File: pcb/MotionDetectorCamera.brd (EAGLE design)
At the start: 100 x 80 mm, 80 parts, among them U1 AT25XV041B-SSHV-T_AT25XV041B-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, U2 TPS62801X_TPS6280X, U3 TPS62801X_TPS6280X, U4 TPS6380X_TPS6380X, U5 LATTICE-SEMICONDUCTOR---ICE40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, U6 MICRON---MT48H32M16LFB4-6-IT: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, X1 CON-COAX_734120110, X10 CON-COAX_734120110, X2 CON-COAX_734120110, X3 CON-COAX_734120110, X4 CON-COAX_734120110, X5 CON-COAX_734120110, X6 CON-COAX_734120110, X7 CON-COAX_734120110, X8 CON-COAX_734120110, X9 CON-COAX_734120110, Y1 SIT8021AI-J4-XXS-12.000000E_S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

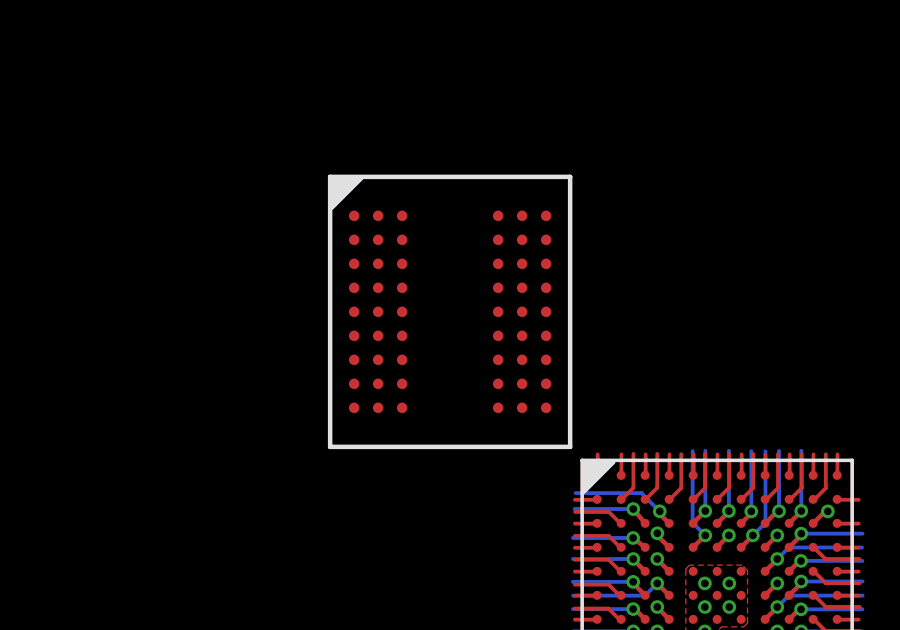
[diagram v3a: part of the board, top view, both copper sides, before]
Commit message: Broke out RAM pins
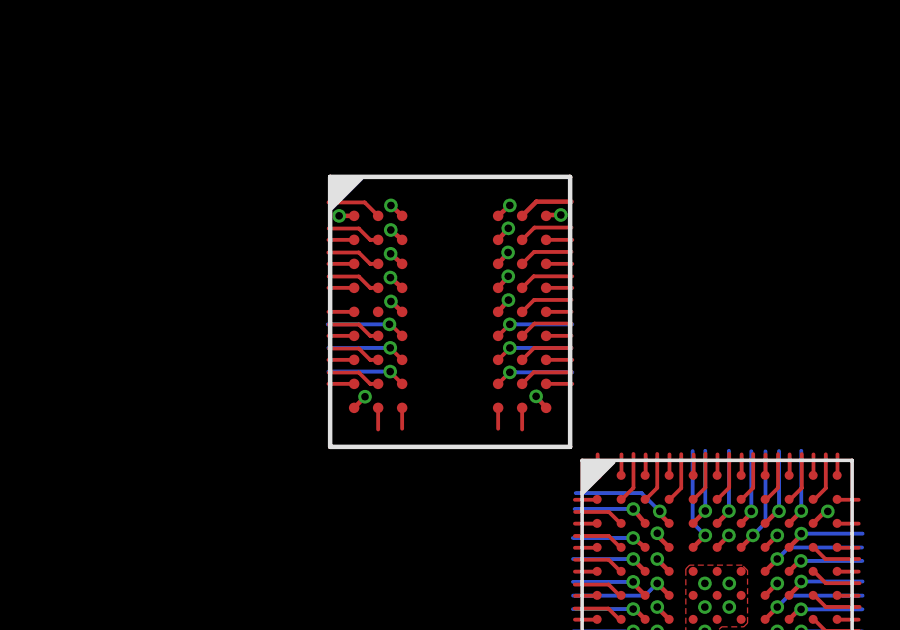
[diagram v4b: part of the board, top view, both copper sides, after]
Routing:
- net GND: track 7.50 -> 11.1 mm, vias 5 -> 12
- net 1V8: track 7.19 -> 10.8 mm, vias 5 -> 12
- net RAM_CKE: track 0.00 -> 2.64 mm, vias 0 -> 1
- net RAM_A6: track 0.00 -> 2.63 mm, vias 0 -> 1
- net RAM_CAS_: track 0.00 -> 2.63 mm, vias 0 -> 1
- net RAM_A0: track 0.00 -> 2.63 mm, vias 0 -> 1
- net RAM_A9: track 0.00 -> 2.62 mm, vias 0 -> 1
- net RAM_BA0: track 0.00 -> 2.62 mm, vias 0 -> 1
- net RAM_DQ0: track 0.00 -> 1.84 mm
- net RAM_DQ15: track 0.00 -> 1.84 mm
- net RAM_DQ6: track 0.00 -> 1.83 mm
- net RAM_DQ11: track 0.00 -> 1.82 mm
- net RAM_DQ2: track 0.00 -> 1.82 mm
- net RAM_RAS_: track 0.00 -> 1.82 mm
- net RAM_DQ4: track 0.00 -> 1.81 mm
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
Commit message: Commit before attempting to rotate RAM 45 degrees
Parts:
- moved U6 3.61 mm to (47.6, 48.5)

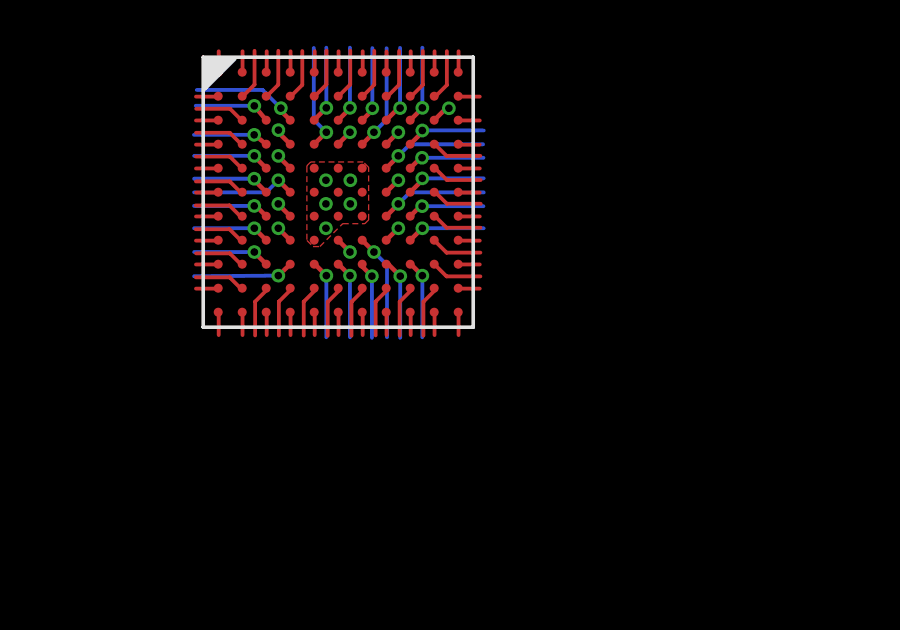
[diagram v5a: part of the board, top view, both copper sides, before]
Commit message: Connected VCC_SPI to 1V8
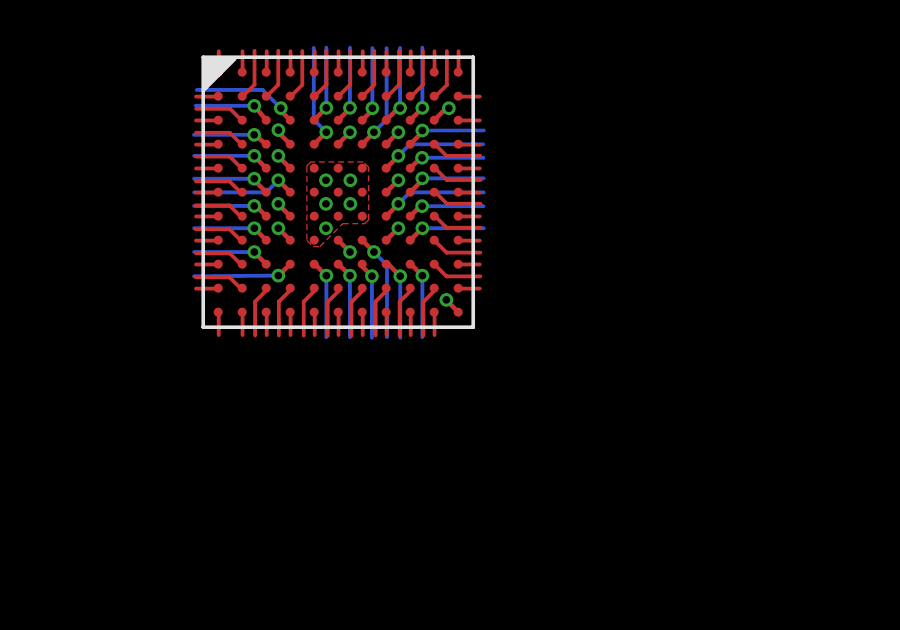
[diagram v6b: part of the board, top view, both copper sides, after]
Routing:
- net 1V8: vias 12 -> 13
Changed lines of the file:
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@@
 <wire x1="59.159" y1="34.984" x2="59.5503" y2="34.5927" width="0.1524" layer="1"/>
 <wire x1="59.5503" y1="34.5927" x2="59.5503" y2="34.58971875" width="0.1524" layer="1"/>
-<wire x1="63.17" y1="31.822" x2="63.17" y2="32.482" width="0.127" layer="1"/>
-<polygon width="0.1524" layer="15" rank="0">
-<vertex x="56.769" y="36.6014"/>
-<vertex x="56.769" y="35.9664"/>
-<vertex x="56.9722" y="35.7632"/>
-<vertex x="57.6326" y="35.7632"/>
-<vertex x="57.6326" y="31.75"/>
-<vertex x="59.9694" y="31.75"/>
-<vertex x="59.9694" y="35.0266"/>
-<vertex x="59.944" y="35.052"/>
-<vertex x="60.706" y="35.814"/>
-<vertex x="60.706" y="36.576"/>
-<vertex x="60.8076" y="36.6776"/>
-<vertex x="61.5188" y="36.6776"/>
-<vertex x="61.5188" y="37.2872"/>
-<vertex x="61.468" y="37.338"/>
-<vertex x="60.7568" y="37.338"/>
-<vertex x="59.2328" y="38.862"/>
-<vertex x="59.2328" y="39.3954"/>
-<vertex x="57.7088" y="39.3954"/>
-<vertex x="57.7088" y="38.5318"/>
-<vertex x="57.3786" y="38.2016"/>
-<vertex x="56.8198" y="38.2016"/>
-<vertex x="56.8198" y="37.5158"/>
-<vertex x="56.7944" y="37.4904"/>
-<vertex x="57.6072" y="37.4904"/>
-<vertex x="57.6326" y="37.465"/>
-<vertex x="57.6326" y="36.6522"/>
-<vertex x="57.5818" y="36.6014"/>
-</polygon>
 <wire x1="50.8428" y1="51.7232" x2="50.8721" y2="51.7525" width="0.1524" layer="1"/>
 <wire x1="50.8721" y1="51.7525" x2="51.4096" y2="51.7525" width="0.1524" layer="1"/>
@@
 <vertex x="51.8922" y="53.1876"/>
 </polygon>
-<wire x1="63.17" y1="32.482" x2="63.159" y2="32.584" width="0" layer="19" extent="1-1"/>
-<wire x1="59.5503" y1="34.58971875" x2="63.159" y2="32.584" width="0" layer="19" extent="1-1"/>
-<wire x1="50.8428" y1="45.3232" x2="57.1627" y2="37.7952" width="0" layer="19" extent="1-1"/>
-<wire x1="14.9834" y1="59.7408" x2="45.638790625" y2="51.328390625" width="0" layer="19" extent="16-16"/>
-<wire x1="14.9834" y1="60.7822" x2="14.9834" y2="59.7408" width="0" layer="19" extent="16-16"/>
+<wire x1="59.9694" y1="35.0266" x2="59.944" y2="35.052" width="0.1524" layer="15"/>
+<wire x1="63.159" y1="32.584" x2="62.7634" y2="32.9946" width="0.1524" layer="1"/>
+<via x="62.7634" y="32.9946" extent="1-16" drill="0.254"/>
+<polygon width="0.1524" layer="15" rank="0">
+<vertex x="56.769" y="36.6014"/>
+<vertex x="56.769" y="35.9664"/>
+<vertex x="56.9722" y="35.7632"/>
+<vertex x="57.6326" y="35.7632"/>
+<vertex x="57.6326" y="31.75"/>
+<vertex x="63.7032" y="31.75"/>
+<vertex x="63.8302" y="31.877"/>
+<vertex x="63.8302" y="33.5788"/>
+<vertex x="63.8048" y="33.6042"/>
+<vertex x="62.3305375" y="33.6042"/>
+<vertex x="60.706" y="35.2287375"/>
+<vertex x="60.706" y="36.576"/>
+<vertex x="60.8076" y="36.6776"/>
+<vertex x="61.5188" y="36.6776"/>
+<vertex x="61.5188" y="37.2872"/>
+<vertex x="61.468" y="37.338"/>
+<vertex x="60.7568" y="37.338"/>
+<vertex x="59.2328" y="38.862"/>
+<vertex x="59.2328" y="39.3954"/>
+<vertex x="57.7088" y="39.3954"/>
+<vertex x="57.7088" y="38.5318"/>
+<vertex x="57.3786" y="38.2016"/>
+<vertex x="56.8198" y="38.2016"/>
+<vertex x="56.8198" y="37.5158"/>
+<vertex x="56.7944" y="37.4904"/>
+<vertex x="57.6072" y="37.4904"/>
+<vertex x="57.6326" y="37.465"/>
+<vertex x="57.6326" y="36.6522"/>
+<vertex x="57.5818" y="36.6014"/>
+</polygon>
+<wire x1="14.9834" y1="59.7408" x2="14.9834" y2="60.7822" width="0" layer="19" extent="16-16"/>
 <wire x1="6.1214" y1="60.0964" x2="14.9834" y2="59.7408" width="0" layer="19" extent="16-16"/>
 <wire x1="5.8014" y1="61.3664" x2="6.1214" y2="60.0964" width="0" layer="19" extent="16-16"/>
-<wire x1="65.682" y1="-28.912" x2="63.17" y2="31.822" width="0" layer="19" extent="1-1"/>
+<wire x1="45.638790625" y1="51.328390625" x2="14.9834" y2="59.7408" width="0" layer="19" extent="16-16"/>
+<wire x1="57.1627" y1="37.7952" x2="50.8428" y2="45.3232" width="0" layer="19" extent="1-1"/>
+<wire x1="65.682" y1="-28.912" x2="63.159" y2="32.584" width="0" layer="19" extent="1-1"/>
 <wire x1="66.182" y1="-31.412" x2="65.682" y2="-28.912" width="0" layer="19" extent="1-1"/>
 <wire x1="66.182" y1="-32.912" x2="66.182" y2="-31.412" width="0" layer="19" extent="1-1"/>

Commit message: Cleaned up some RAM wiring
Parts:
- moved U6 3.52 mm to (50.1, 46.0)
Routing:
- net RAM_A3: track 0.70 -> 2.78 mm
- net RAM_A4: track 1.41 -> 3.48 mm
- net RAM_A2: track 0.72 -> 1.86 mm
- net RAM_A5: track 0.72 -> 1.82 mm

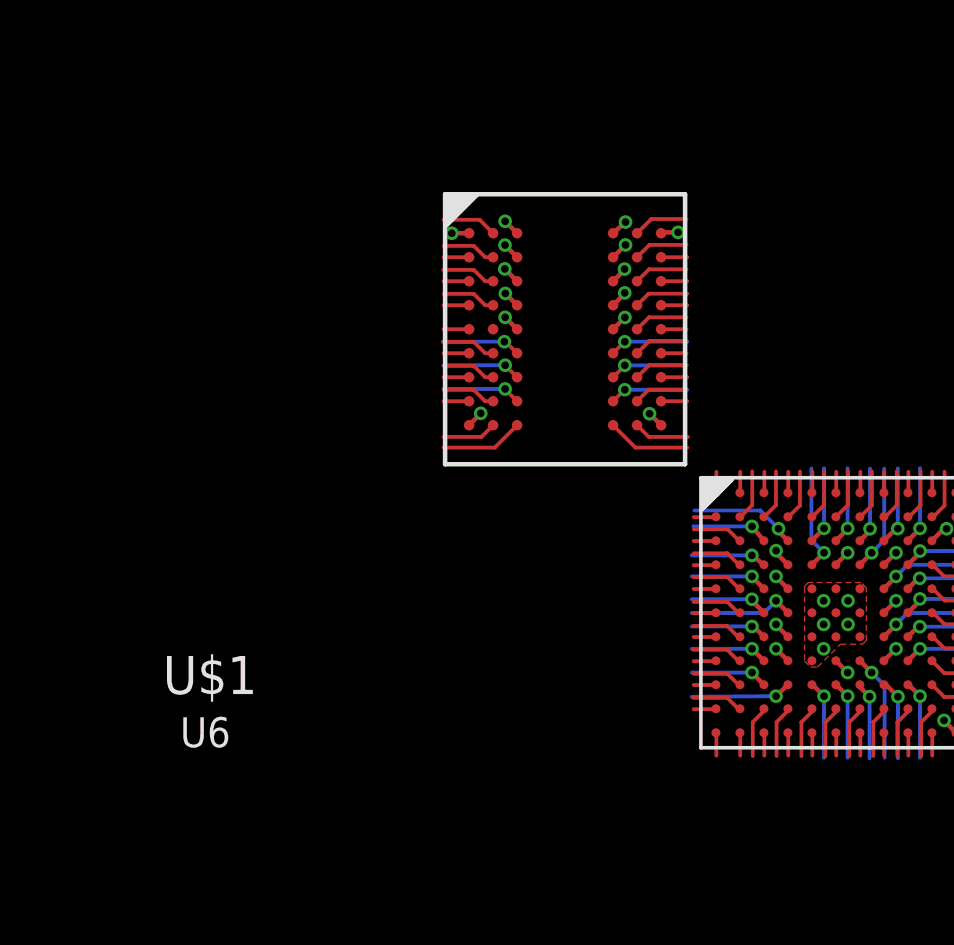
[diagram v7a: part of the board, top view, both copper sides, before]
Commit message: Successfully rotated RAM
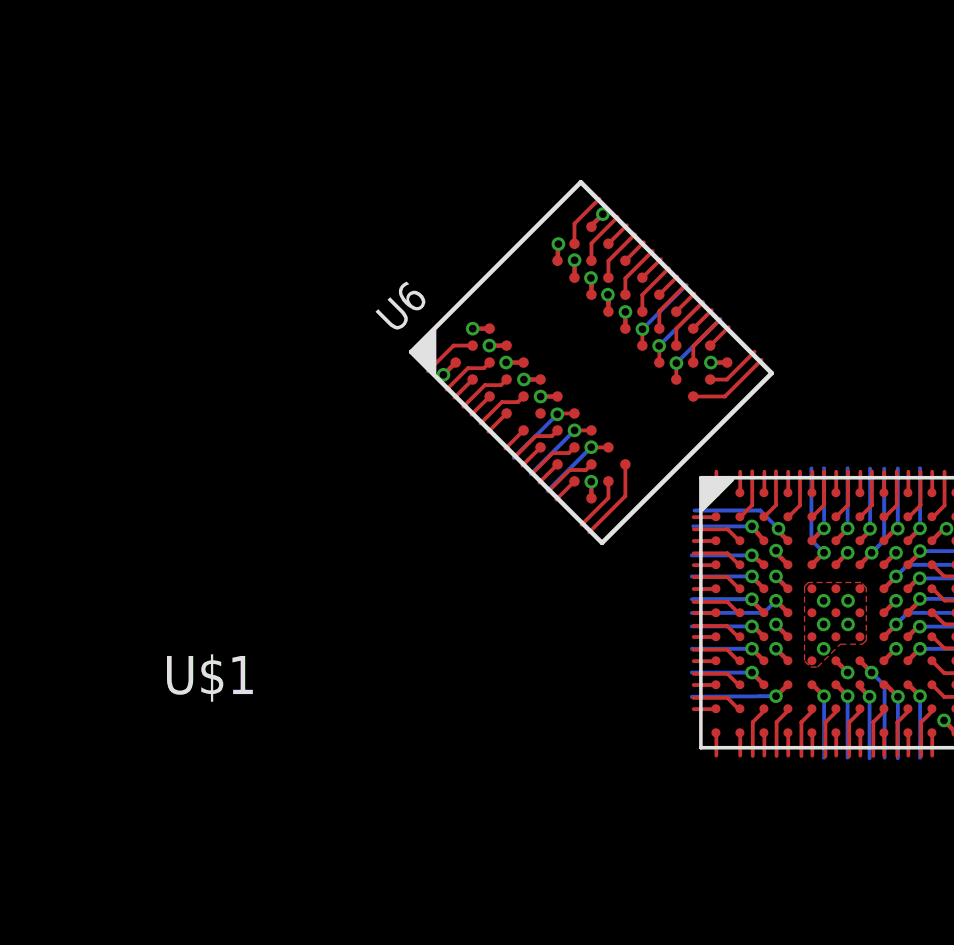
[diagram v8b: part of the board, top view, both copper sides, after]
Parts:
- moved U6 1.42 mm to (51.0, 44.9), turned to 45 degrees
